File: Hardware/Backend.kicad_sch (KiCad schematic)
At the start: 14 parts, among them K1 G6DN-1A-L_DC5, K2 G6DN-1A-L_DC5, Q1 BC547, Q2 BC547, U7 CNY17-4, U8 CNY17-4

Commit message: schematic update
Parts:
- added F1: 2A, symbol Device:Fuse
- added J2: Conn_01x03, symbol Connector_Generic:Conn_01x03
- R10, R14: value 1k -> 470
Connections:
- net 230v AC: now also F1.1
- net FAN_LIVE: now reaches K1.5 (NO)
- net FAN_LIVE: now also J2.2 (Pin_2)
- net FAN_CONTROL: now reaches R12.2
- net HEATER_LIVE: now reaches K2.5 (NO)
- net HEATER_LIVE: now also J2.3 (Pin_3)
- net HEATER_CONTROL: now reaches R13.2
- new net: F1.2, J2.1 (Pin_1)

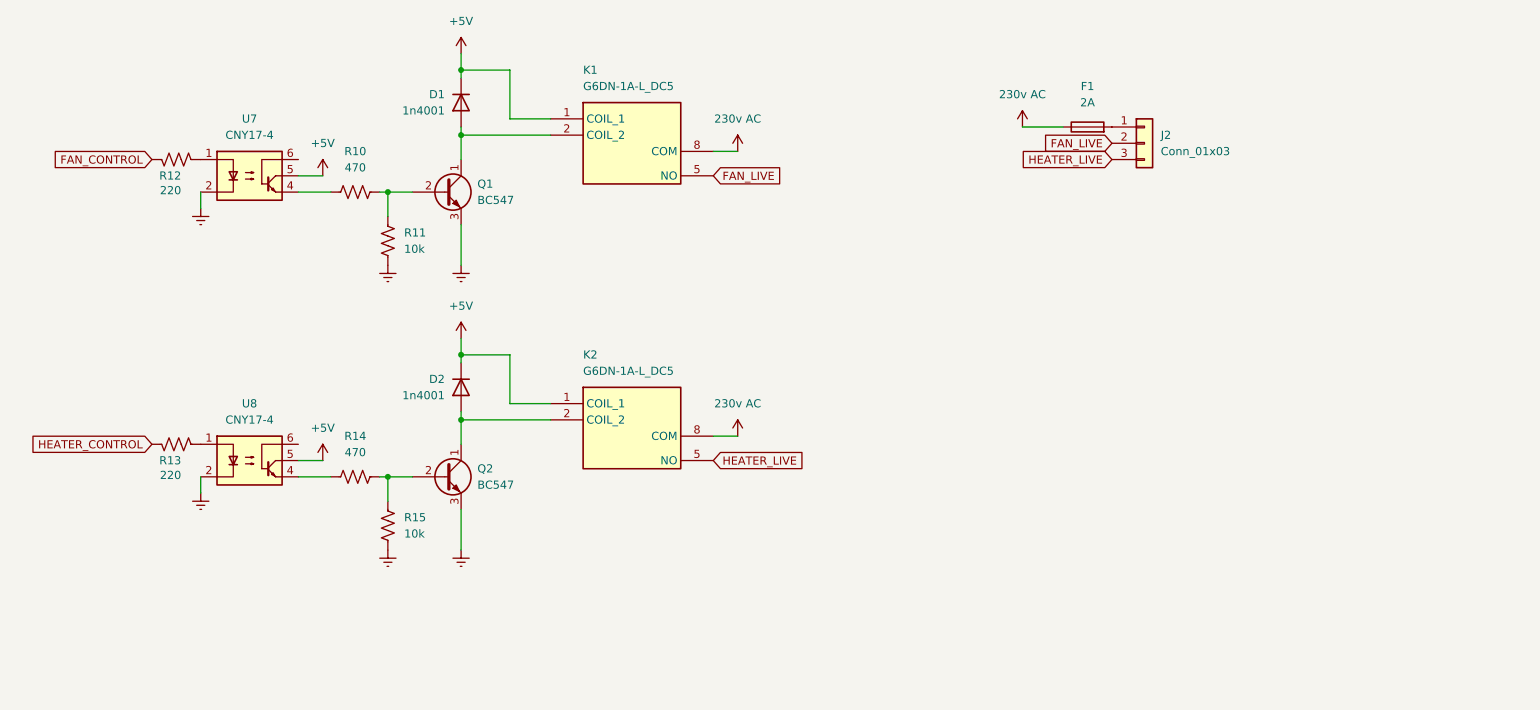
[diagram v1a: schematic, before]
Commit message: Safety features on mains voltage
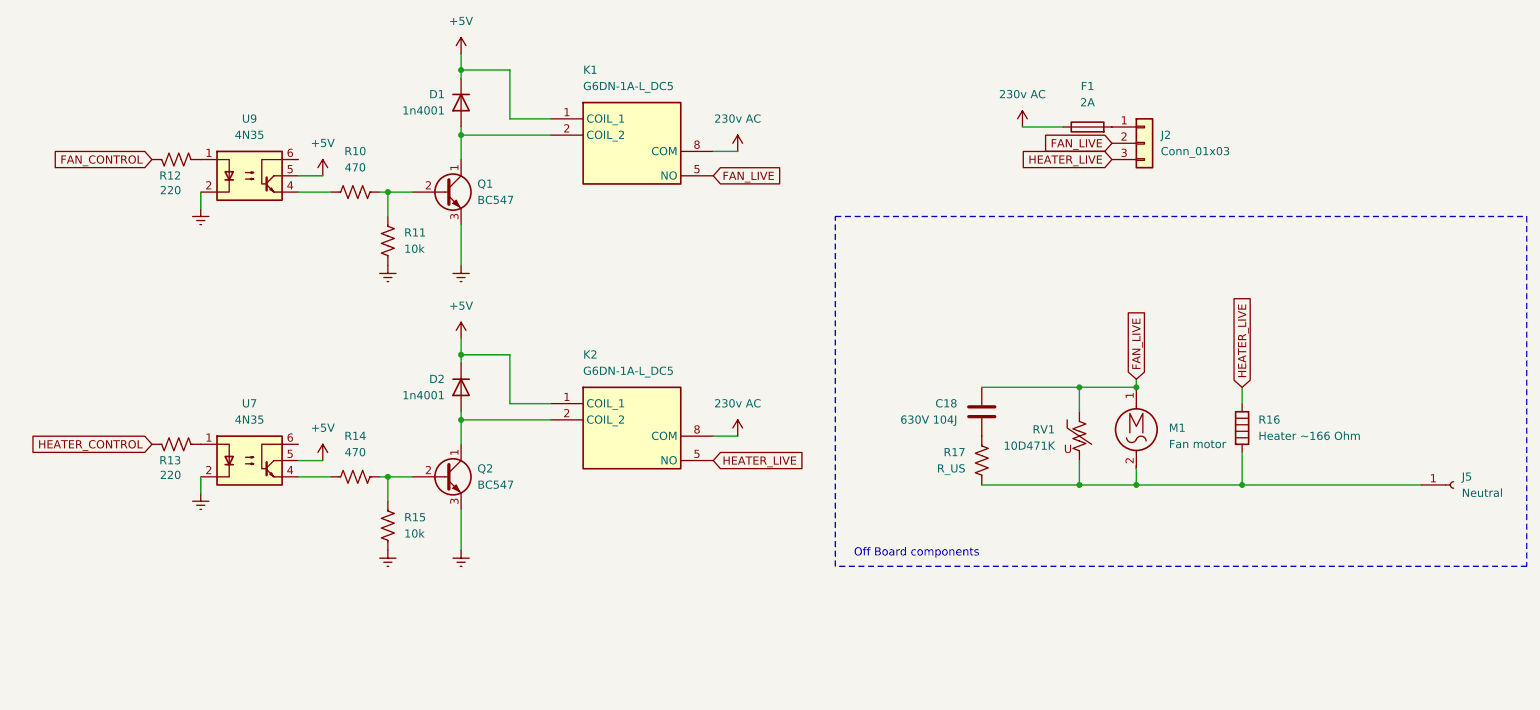
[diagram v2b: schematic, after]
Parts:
- removed U7, U8: CNY17-4, symbol Isolator:CNY17-4
- added C18: 630V 104J, symbol Device:C
- added J5: Neutral, symbol Connector:Conn_01x01_Socket
- added M1: Fan motor, symbol Motor:Motor_AC
- added R16: Heater ~166 Ohm, symbol Device:Heater
- added R17: R_US, symbol Device:R_US
- added RV1: 10D471K, symbol Device:Varistor_US
- added U7, U9: 4N35, Package_DIP:DIP-6_W7.62mm, symbol Isolator:4N35
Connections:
- net +5V: now also U7.5, U9.5
- net Earth: now also U7.2, U9.2
- net FAN_LIVE: now also C18.1, M1.1, RV1.1
- net HEATER_LIVE: now also R16.1
- net at R12.1: now also U9.1
- net at R13.1: now also U7.1
- net at R10.1: now also U9.4
- net at R14.1: now also U7.4
- new net: J5.1 (Pin_1), M1.2, R16.2, R17.2, RV1.2
- new net: C18.2, R17.1
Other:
- note added: "Off Board components"

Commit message: added footprints
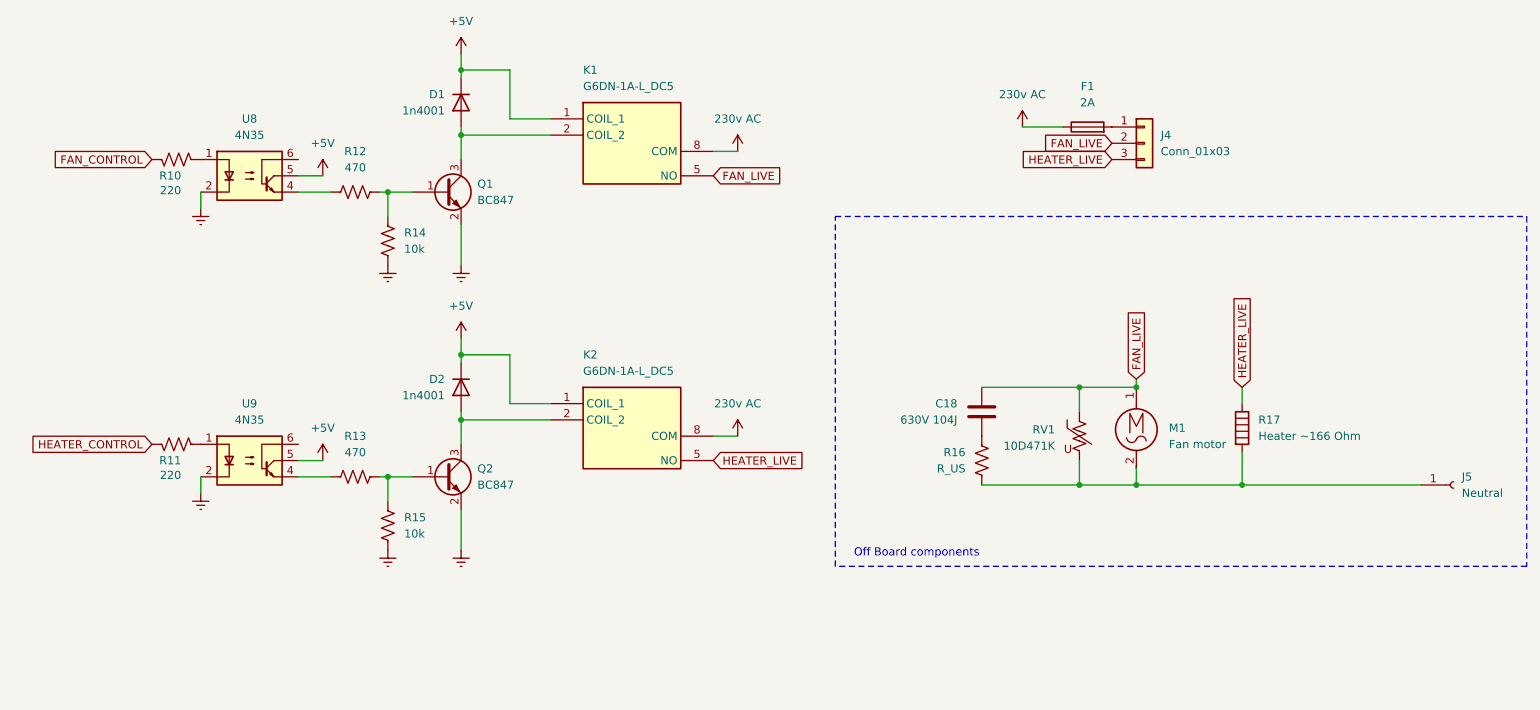
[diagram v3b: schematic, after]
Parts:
- removed Q1, Q2: BC547, Package_TO_SOT_THT:TO-92_Inline, symbol Transistor_BJT:BC547
- added Q1, Q2: BC847, Package_TO_SOT_SMD:SOT-23, symbol Transistor_BJT:BC847
- K1, K2: footprint G6DN-1A-L -> SamacSys_Parts:G6DN-1A-L
- R10: renamed from R12; footprint (none) -> Resistor_SMD:R_0805_2012Metric
- R11: renamed from R13; footprint (none) -> Resistor_SMD:R_0805_2012Metric
- R12: renamed from R10; footprint (none) -> Resistor_SMD:R_0805_2012Metric
- R13: renamed from R14; footprint (none) -> Resistor_SMD:R_0805_2012Metric
- R14: renamed from R11; footprint (none) -> Resistor_SMD:R_0805_2012Metric
- R15: footprint (none) -> Resistor_SMD:R_0805_2012Metric
- U8: renamed from U9; footprint Package_DIP:DIP-6_W7.62mm -> SamacSys_Parts:4N35S
- U9: renamed from U7; footprint Package_DIP:DIP-6_W7.62mm -> SamacSys_Parts:4N35S
- renumbered J2 to J4, R17 to R16, R16 to R17
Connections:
- net Earth: now also Q1.2 (E), Q2.2 (E)
- net at D1.2 (A), K1.2 (COIL_2): now also Q1.3 (C)
- net at R12.2, R14.2: now also Q1.1 (B)
- net at D2.2 (A), K2.2 (COIL_2): now also Q2.3 (C)
- net at R13.2, R15.2: now also Q2.1 (B)

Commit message: Added temperature sensor and I2C setup, started PCB layout
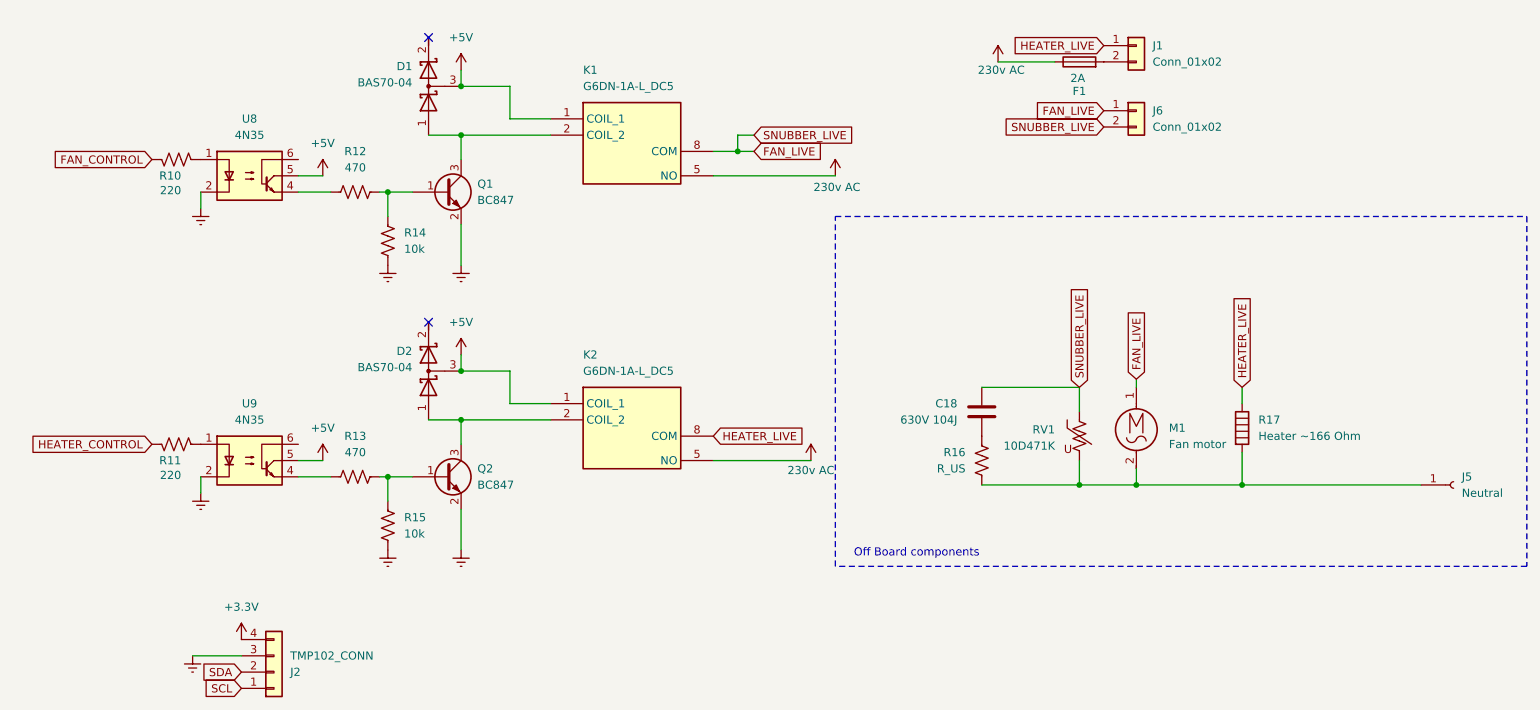
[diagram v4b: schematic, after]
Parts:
- removed D1, D2: 1n4001, symbol Device:D
- removed J4: Conn_01x03, symbol Connector_Generic:Conn_01x03
- added D1, D2: BAS70-04, SamacSys_Parts:SOT97P230X109-3N, symbol Device:D_Schottky_Dual_Series_ACK
- added J1, J6: Conn_01x02, TerminalBlock_Phoenix:TerminalBlock_Phoenix_PT-1,5-2-5.0-H_1x02_P5.00mm_Horizontal, symbol Connector_Generic:Conn_01x02
- added J2: TMP102_CONN, Connector_JST:JST_XH_B4B-XH-AM_1x04_P2.50mm_Vertical, symbol Connector_Generic:Conn_01x04
- F1: footprint (none) -> SamacSys_Parts:WR-FSH_THT_2
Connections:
- net +5V: now also D1.3 (common), D2.3 (common)
- net 230v AC: now also K1.5 (NO), K2.5 (NO); no longer K1.8 (COM), K2.8 (COM)
- net Earth: now also J2.3 (Pin_3)
- net FAN_LIVE: now also K1.8 (COM), J6.1 (Pin_1), J6.2 (Pin_2); no longer K1.5 (NO)
- net HEATER_LIVE: now also K2.8 (COM), J1.1 (Pin_1); no longer K2.5 (NO)
- net at K2.2 (COIL_2), Q2.3 (C): now also D2.1 (A)
- net at K1.2 (COIL_2), Q1.3 (C): now also D1.1 (A)
- net at F1.2: now also J1.2 (Pin_2)
- new net +3.3V: J2.4 (Pin_4)
- new net SCL: J2.1 (Pin_1)
- new net SDA: J2.2 (Pin_2)
- no-connect marks 0 -> 2
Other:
- moved on the sheet: F1
